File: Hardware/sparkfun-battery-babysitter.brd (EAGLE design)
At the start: 33 x 33 mm, 58 parts, among them U1 BQ24075, U2 BQ27441-G1

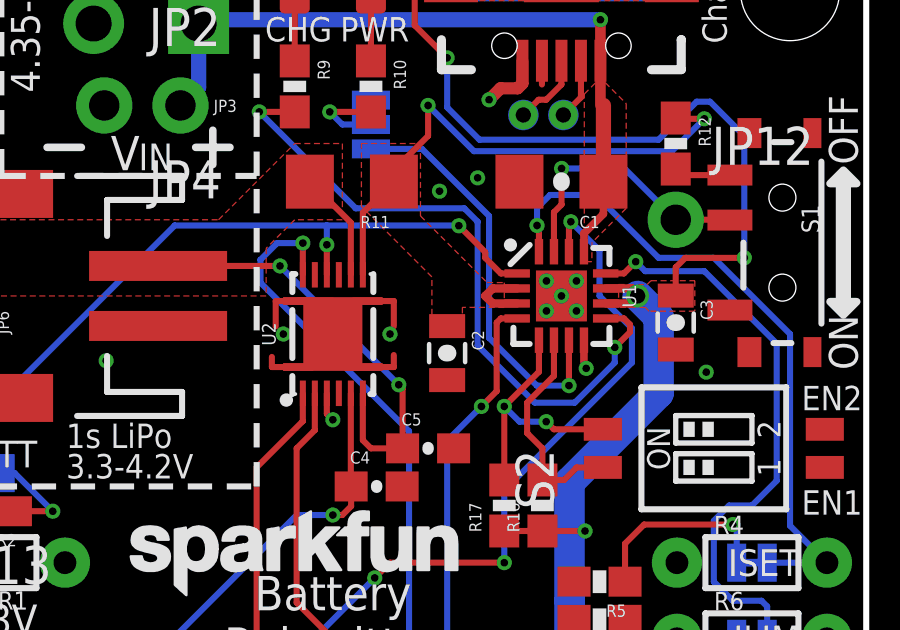
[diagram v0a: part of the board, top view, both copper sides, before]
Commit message: Removing temp library, and updating libs in eagle files.
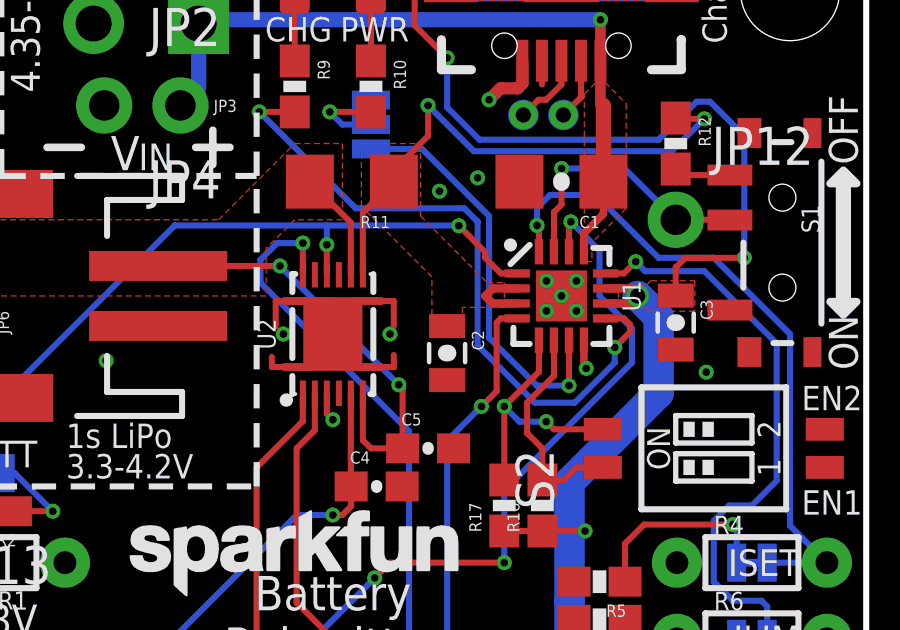
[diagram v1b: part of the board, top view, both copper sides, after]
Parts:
- U1: device battery-management-temp:PVQFN-N16 -> SparkFun-PowerIC:PVQFN-N16
- U2: device battery-management-temp:PDSO-N12 -> SparkFun-PowerIC:PDSO-N12

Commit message: Values Added to 3 Part on .brd/.sch
USB-AB-MICRO-SMD_V03
SW_DIP-2_SMD
RIGHT_ANGLE_SLIDE_SWITCH_SMD
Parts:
- JP1: value (none) -> USB-AB-MICRO-SMD_V03
- S1: value (none) -> RIGHT_ANGLE_SLIDE_SWITCH_SMD
- S2: value (none) -> SW_DIP-2_SMD
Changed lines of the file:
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@@
 <?xml version="1.0" encoding="utf-8"?>
 <!DOCTYPE eagle SYSTEM "eagle.dtd">
-<eagle version="7.5.0">
+<eagle version="7.7.0">
 <drawing>
 <settings>
@@
 <elements>
 <element name="FRAME1" library="SparkFun-Aesthetics" package="CREATIVE_COMMONS" value="FRAME-LETTER" x="-0.635" y="-20.955"/>
-<element name="JP1" library="SparkFun-Connectors" package="USB-AB-MICRO-SMD_V03" value="" x="22.86" y="30.861" rot="R270">
+<element name="JP1" library="SparkFun-Connectors" package="USB-AB-MICRO-SMD_V03" value="USB-AB-MICRO-SMD_V03" x="22.86" y="30.861" rot="R270">
 <attribute name="PROD_ID" value="CONN-11794" x="22.86" y="30.861" size="1.778" layer="27" font="vector" ratio="15" rot="R270" display="off"/>
 </element>
@@
 <element name="STANDOFF2" library="SparkFun-Electromechanical" package="STAND-OFF" value="STAND-OFF" x="2.54" y="2.54"/>
 <element name="STANDOFF4" library="SparkFun-Electromechanical" package="STAND-OFF" value="STAND-OFF" x="30.48" y="2.54"/>
-<element name="S1" library="SparkFun-Electromechanical" package="SWITCH-SPST-SMD-A" value="" x="30.226" y="22.098" rot="R270">
+<element name="S1" library="SparkFun-Electromechanical" package="SWITCH-SPST-SMD-A" value="RIGHT_ANGLE_SLIDE_SWITCH_SMD" x="30.226" y="22.098" rot="R270">
 <attribute name="PROD_ID" value="SWCH-10651" x="30.226" y="22.098" size="1.778" layer="27" rot="R270" display="off"/>
 </element>
@@
 <element name="FID1" library="SparkFun-Aesthetics" package="FIDUCIAL-1X2" value="FIDUCIAL1X2" x="0.889" y="28.194"/>
 <element name="FID2" library="SparkFun-Aesthetics" package="FIDUCIAL-1X2" value="FIDUCIAL1X2" x="29.21" y="5.08"/>
-<element name="S2" library="SparkFun-Electromechanical" package="DIPSWITCH-02-50MIL" value="" x="27.94" y="15.24" rot="R90">
+<element name="S2" library="SparkFun-Electromechanical" package="DIPSWITCH-02-50MIL" value="SW_DIP-2_SMD" x="27.94" y="15.24" rot="R90">
 <attribute name="PROD_ID" value="SWCH-13215" x="27.94" y="15.24" size="1.778" layer="27" rot="R90" display="off"/>
 </element>
